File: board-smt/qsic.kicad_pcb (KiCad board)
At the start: 4 copper layers, 214.1 x 131.7 mm, 243 parts, among them CON1 SD 0, CON2 SD 1, P1 USB_A, P2 Indicator Panel, Q201 Dual_NMOS, Q202 Dual_NMOS, Q203 Dual_NMOS, Q204 Dual_NMOS, Q205 Dual_NMOS, Q206 Dual_NMOS, Q207 Dual_NMOS, Q208 Dual_NMOS, Q209 Dual_NMOS, Q210 Dual_NMOS, Q211 Dual_NMOS, Q212 Dual_NMOS, Q301 Dual_NMOS, Q302 Dual_NMOS, Q303 Dual_NMOS, Q304 Dual_NMOS, Q305 Dual_NMOS, Q306 Dual_NMOS, Q307 Dual_NMOS, U201 CMP401, U202 CMP401, U203 CMP401, U204 CMP401, U205 CMP401, U206 CMP401, U301 CMP401, U302 CMP401, U303 CMP401, U304 CMP401, U305 CMP401, U306 AOZ3010PI, U307 AOZ3010PI, U308 RT8288A, U309 SC189, U401 XC7A75T-CSG324, U501 IS43TR16128B, U601 MAX3033E

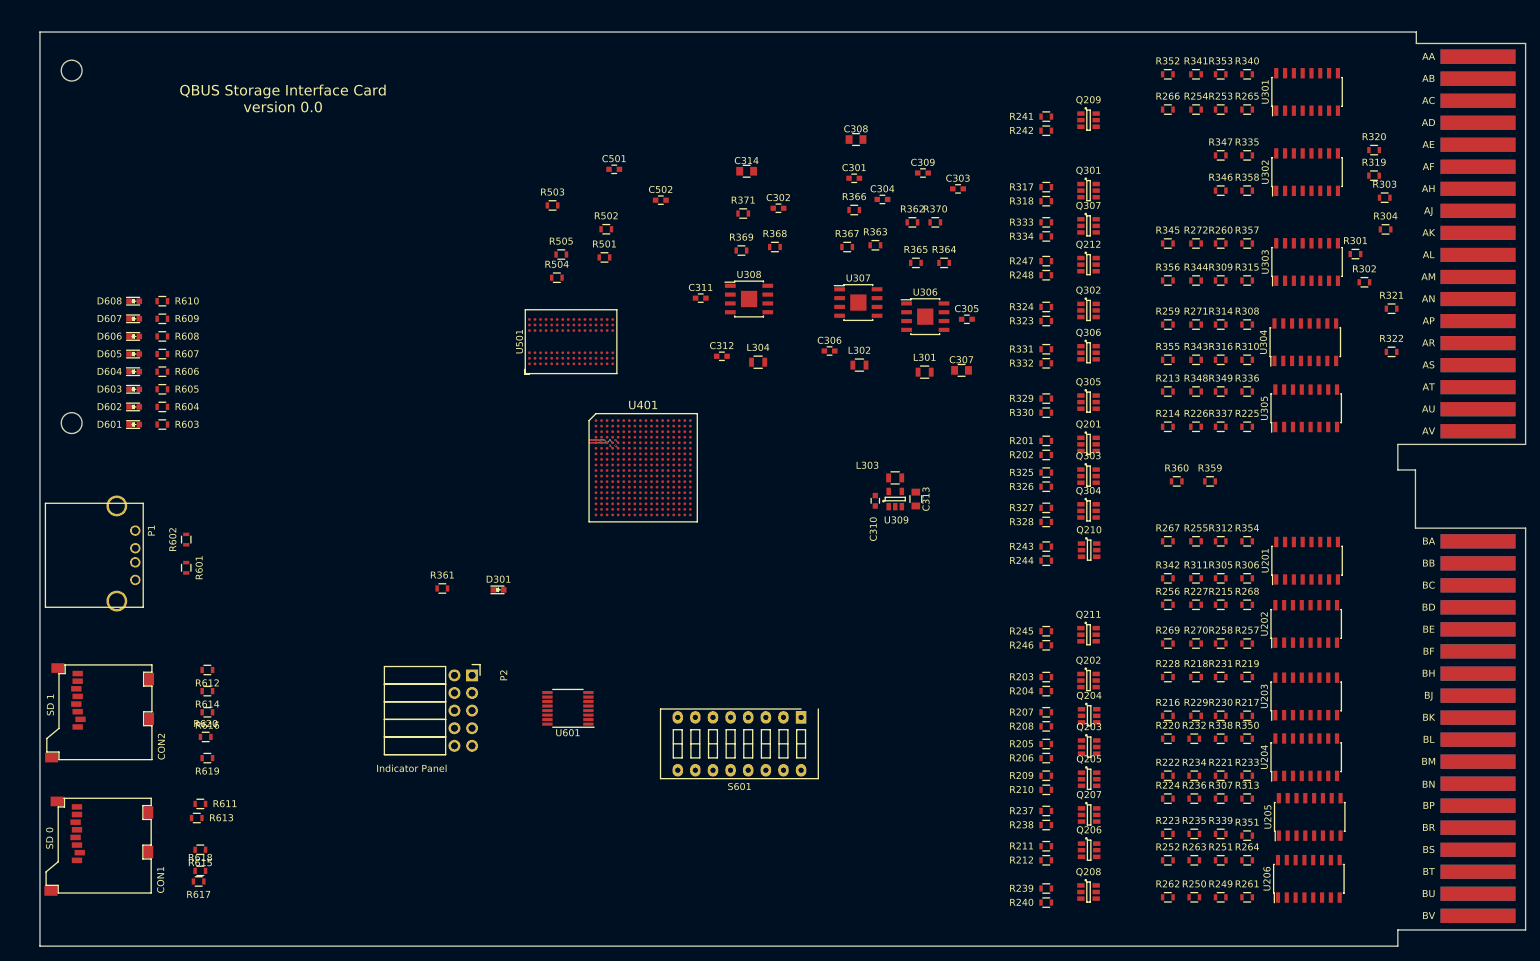
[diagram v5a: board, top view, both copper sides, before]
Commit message: Worked on the board layout for the bus receivers.
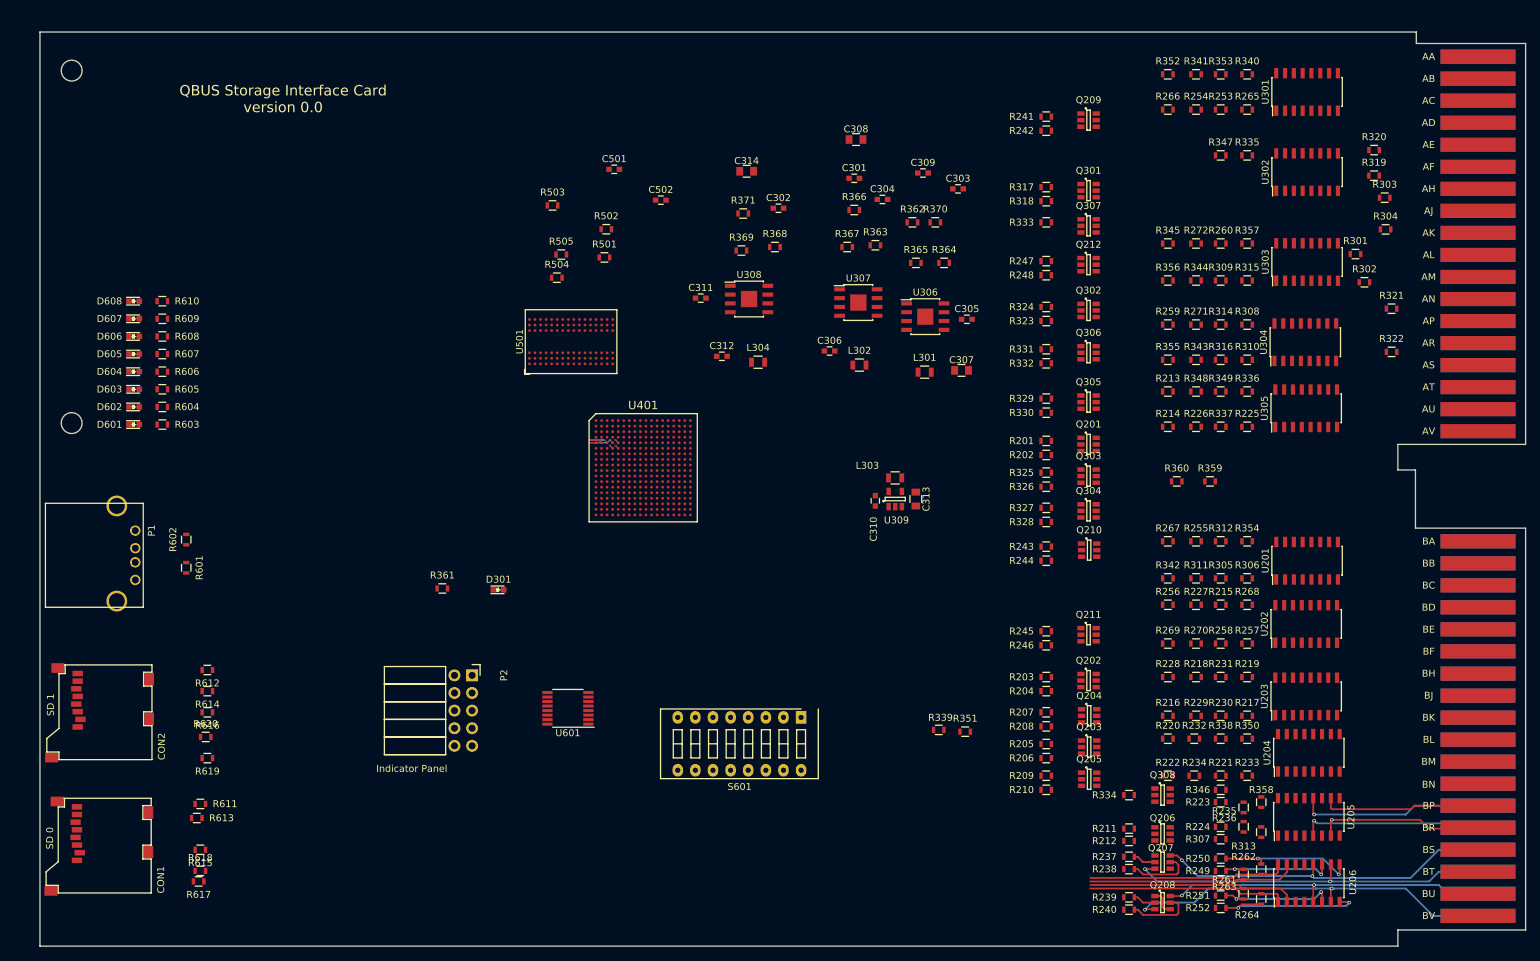
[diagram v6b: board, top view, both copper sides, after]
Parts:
- added Q308: Dual_NMOS, TO_SOT_Packages_SMD:SOT-23-6, F.Cu at (194.1, 135.4)
- moved R358 88.2 mm to (208.3, 136.4), turned to 270 degrees
- moved R346 86.4 mm to (202.4, 134.6), turned to 180 degrees
- moved R334 81.4 mm to (189.2, 135.4)
- moved R339 43.3 mm to (161.8, 126.0)
- moved R351 43.3 mm to (165.6, 126.2)
- moved R262 14.1 mm to (208.3, 146.1), turned to 270 degrees
- moved R237 13.6 mm to (189.2, 144.3)
- moved R238 13.5 mm to (189.2, 146.1)
- moved Q207 12.6 mm to (194.1, 145.0)
- moved R212 12.3 mm to (189.2, 142.0)
- moved R211 12.2 mm to (189.2, 140.2)
- moved R239 12.0 mm to (189.2, 150.1)
- moved R240 12.0 mm to (189.2, 151.9)
- moved Q206 10.8 mm to (194.1, 141.0)
- moved Q208 10.8 mm to (194.1, 150.9)
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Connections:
- Q307 pad 3: /Bus Control/BIRQ7 -> (no net)
- Q307 pad 4: GND -> (no net)
- Q307 pad 5: Net-(Q307-Pad5) -> (no net)
- R334 pad 1: Net-(Q307-Pad5) -> Net-(Q308-Pad2)
- U205 pad 1: /RREF -> /REVNT
- U205 pad 10: /Bus Control/BEVNT -> /Bus Control/BIRQ7
- U205 pad 11: Net-(R224-Pad1) -> Net-(R223-Pad1)
- U205 pad 12: /BDAL11 -> /BDAL10
- U205 pad 15: /Address/Data/RDAL11 -> /Address/Data/RDAL10
- U205 pad 16: /REVNT -> /RIRQ7
- U205 pad 2: /Address/Data/RDAL10 -> /Address/Data/RDAL11
- U205 pad 5: /BDAL10 -> /BDAL11
- U205 pad 6: Net-(R223-Pad1) -> Net-(R224-Pad1)
- U205 pad 7: /Bus Control/BREF -> /Bus Control/BEVNT
- U205 pad 8: Net-(R339-Pad1) -> Net-(R307-Pad2)
- U205 pad 9: Net-(R307-Pad2) -> Net-(R346-Pad1)
- U206 pad 1: /Address/Data/RDAL13 -> /Address/Data/RDAL15
- U206 pad 10: /BDAL14 -> /BDAL13
- U206 pad 11: Net-(R252-Pad1) -> Net-(R249-Pad1)
- U206 pad 12: /BDAL15 -> /BDAL12
- U206 pad 15: /Address/Data/RDAL15 -> /Address/Data/RDAL12
- U206 pad 16: /Address/Data/RDAL14 -> /Address/Data/RDAL13
- U206 pad 2: /Address/Data/RDAL12 -> /Address/Data/RDAL14
- U206 pad 5: /BDAL12 -> /BDAL14
- U206 pad 6: Net-(R249-Pad1) -> Net-(R251-Pad1)
- U206 pad 7: /BDAL13 -> /BDAL15
- U206 pad 8: Net-(R250-Pad1) -> Net-(R252-Pad1)
- U206 pad 9: Net-(R251-Pad1) -> Net-(R250-Pad1)
- U302 pad 2: /RIRQ7 -> /RREF
- U302 pad 5: /Bus Control/BIRQ7 -> /Bus Control/BREF
- U302 pad 6: Net-(R346-Pad1) -> Net-(R339-Pad1)
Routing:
- net /BDAL15: track 0.00 -> 54.5 mm, vias 0 -> 2
- net /BDAL13: track 0.00 -> 53.5 mm, vias 0 -> 2
- net /BDAL12: track 0.00 -> 49.3 mm, vias 0 -> 2
- net /BDAL14: track 0.00 -> 48.2 mm, vias 0 -> 2
- net /Address/Data/RDAL14: track 0.00 -> 29.9 mm
- net /Address/Data/RDAL12: track 0.00 -> 29.9 mm
- net /Address/Data/RDAL15: track 0.00 -> 28.9 mm
- net /Address/Data/RDAL13: track 0.00 -> 28.4 mm
- net /BDAL10: track 0.00 -> 26.6 mm, vias 0 -> 1
- net /BDAL11: track 0.00 -> 26.3 mm, vias 0 -> 1
- net /Bus Control/BEVNT: track 0.00 -> 23.8 mm, vias 0 -> 1
- net Net-(R252-Pad1): track 0.00 -> 23.1 mm, vias 0 -> 2
- net /Bus Control/BIRQ7: track 0.00 -> 22.9 mm
- net Net-(R250-Pad1): track 0.00 -> 19.8 mm, vias 0 -> 2
- net Net-(R249-Pad1): track 0.00 -> 16.9 mm, vias 0 -> 2
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
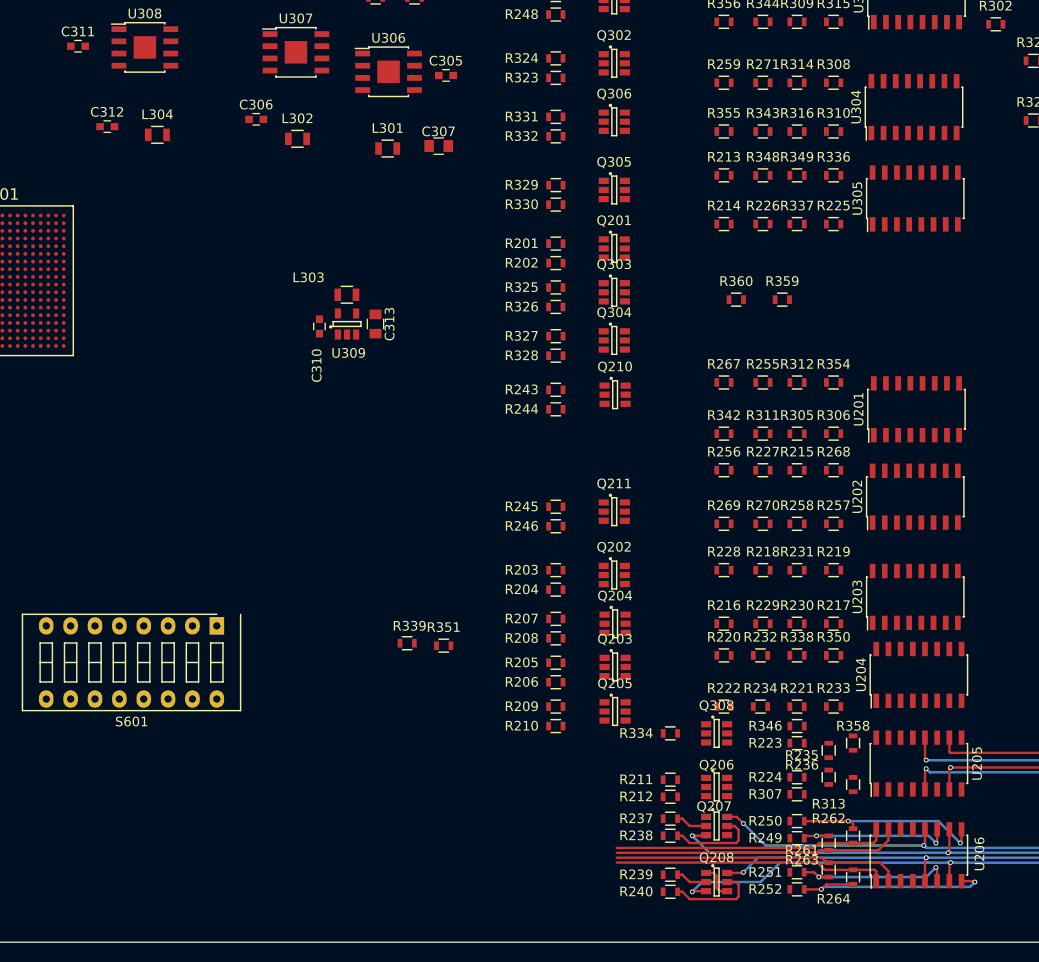
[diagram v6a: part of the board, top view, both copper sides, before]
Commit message: Moved comparator power connections to separate symbols.
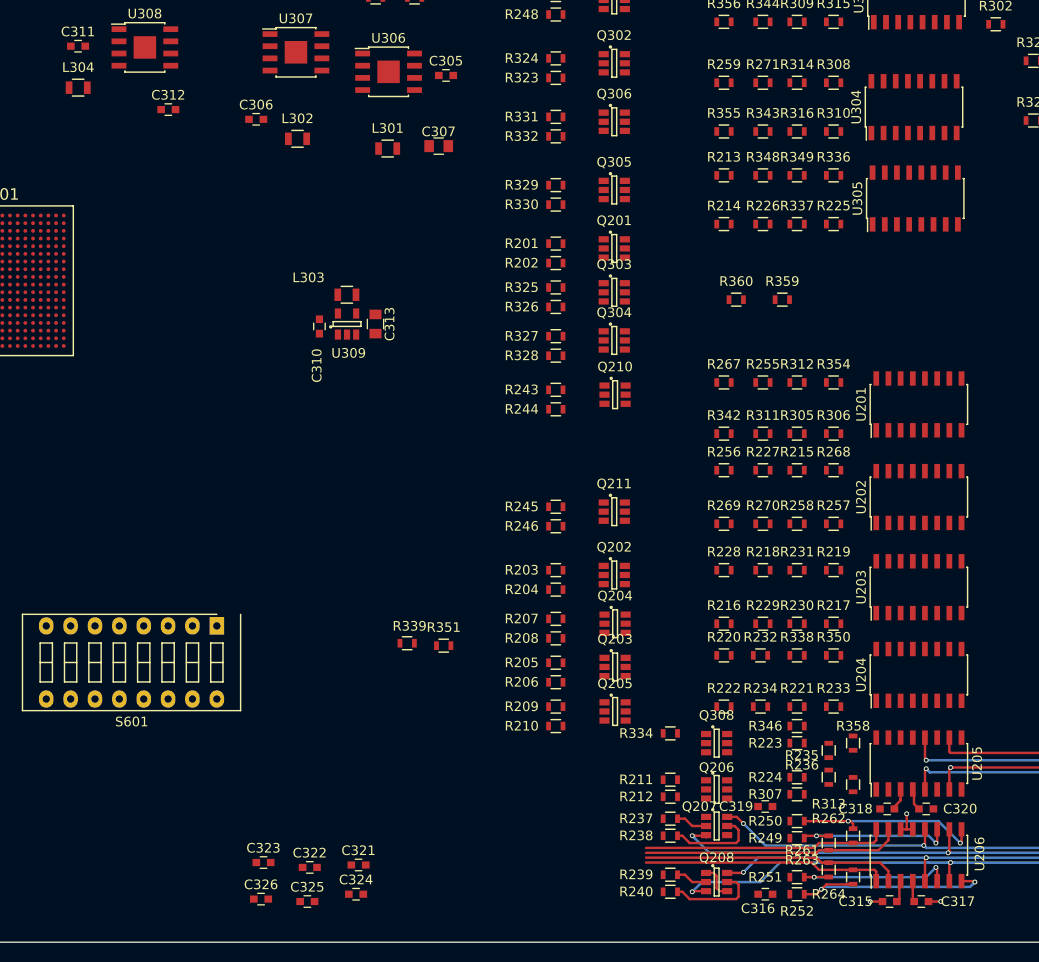
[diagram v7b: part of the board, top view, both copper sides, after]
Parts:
- added C315: 100nF, Capacitors_SMD:C_0603, F.Cu at (212.1, 152.9)
- added C316: 100nF, Capacitors_SMD:C_0603, F.Cu at (199.1, 152.1)
- added C317: 100nF, Capacitors_SMD:C_0603, F.Cu at (215.4, 152.9)
- added C318: 100nF, Capacitors_SMD:C_0603, F.Cu at (211.8, 143.3)
- added C319: 100nF, Capacitors_SMD:C_0603, F.Cu at (199.1, 143.0)
- added C320: 100nF, Capacitors_SMD:C_0603, F.Cu at (215.9, 143.3)
- added C321: 100nF, Capacitors_SMD:C_0603, F.Cu at (156.7, 149.1)
- added C322: 100nF, Capacitors_SMD:C_0603, F.Cu at (151.7, 149.4)
- added C323: 100nF, Capacitors_SMD:C_0603, F.Cu at (146.8, 148.8)
- added C324: 100nF, Capacitors_SMD:C_0603, F.Cu at (156.5, 152.1)
- added C325: 100nF, Capacitors_SMD:C_0603, F.Cu at (151.4, 152.9)
- added C326: 100nF, Capacitors_SMD:C_0603, F.Cu at (146.6, 152.7)
- R335, R336: value R -> 20kΩ
- R347, R348: value R -> 340kΩ
- moved L304 9.61 mm to (127.5, 68.1)
- moved C312 6.61 mm to (136.9, 70.4)
- moved U203 1.09 mm to (215.1, 120.1)
- moved Q308 1.02 mm to (194.1, 136.4)
- moved U201 0.57 mm to (215.1, 101.1)
- moved R251 0.51 mm to (202.4, 150.4)
- moved R252 0.51 mm to (202.4, 152.1)
- moved U202 0.38 mm to (215.1, 110.7)
- moved Q206 0.25 mm to (194.1, 141.2)
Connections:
- R202 pad 1: Net-(Q201-Pad5) -> /Address/Data/TDAL1
- R202 pad 2: /Address/Data/TDAL1 -> Net-(Q201-Pad5)
- R219 pad 1: Net-(R219-Pad1) -> +1V5
- R219 pad 2: +1V5 -> Net-(R219-Pad2)
- R231 pad 1: Net-(R219-Pad1) -> Net-(R219-Pad2)
- R235 pad 2: /Address/Data/RDAL10 -> Net-(R235-Pad2)
- R262 pad 1: Net-(R250-Pad1) -> /Address/Data/RDAL13
- R262 pad 2: /Address/Data/RDAL13 -> Net-(R250-Pad1)
- R311 pad 1: Net-(R305-Pad2) -> /RPOK
- R311 pad 2: /RPOK -> Net-(R305-Pad2)
- R312 pad 1: Net-(R306-Pad2) -> /RDCOK
- R312 pad 2: /RDCOK -> Net-(R306-Pad2)
- R313 pad 1: Net-(R307-Pad2) -> /REVNT
- R313 pad 2: /REVNT -> Net-(R307-Pad2)
- R314 pad 1: Net-(R308-Pad2) -> /RHALT
- R314 pad 2: /RHALT -> Net-(R308-Pad2)
- R315 pad 1: Net-(R309-Pad2) -> /RIAKI
- R315 pad 2: /RIAKI -> Net-(R309-Pad2)
- R316 pad 1: Net-(R310-Pad2) -> /RDMGI
- R316 pad 2: /RDMGI -> Net-(R310-Pad2)
- R355 pad 1: Net-(R343-Pad1) -> /RIRQ4
- R355 pad 2: /RIRQ4 -> Net-(R343-Pad1)
- R356 pad 1: Net-(R344-Pad1) -> /RIRQ5
- R356 pad 2: /RIRQ5 -> Net-(R344-Pad1)
- R357 pad 1: Net-(R345-Pad1) -> /RIRQ6
- R357 pad 2: /RIRQ6 -> Net-(R345-Pad1)
- R358 pad 1: Net-(R346-Pad1) -> /RIRQ7
- R358 pad 2: /RIRQ7 -> Net-(R346-Pad1)
- R601 pad 1: /I/O/USB_D+ -> /I/O/USB_D-
- R602 pad 1: /I/O/USB_D- -> /I/O/USB_D+
- U203 pad 9: Net-(R219-Pad1) -> Net-(R219-Pad2)
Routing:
- net /Address/Data/RDAL13: track 28.4 -> 1.51 mm
- net Net-(R250-Pad1): track 19.8 -> 43.7 mm
- net GND: track 7.26 -> 12.7 mm, vias 1 -> 4
- net +3V3: track 0.00 -> 4.60 mm
- net +5V: track 0.00 -> 4.48 mm
- net /Address/Data/RDAL14: track 29.9 -> 26.9 mm
- net /Address/Data/RDAL15: track 28.9 -> 25.8 mm
- net /Address/Data/RDAL12: track 29.9 -> 26.8 mm

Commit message: Little fixups
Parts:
- P2: footprint Socket_Strips:Socket_Strip_Angled_2x05 -> Pin_Headers:Pin_Header_Angled_2x05
- moved D601 24.3 mm to (53.8, 59.0)
- moved R603 24.3 mm to (57.9, 59.0)
- moved D602 24.3 mm to (53.8, 56.4)
- moved D604 24.3 mm to (53.8, 51.4)
- moved D606 24.3 mm to (53.8, 46.3)
- moved D608 24.3 mm to (53.8, 41.2)
- moved R604 24.3 mm to (57.9, 56.4)
- moved R606 24.3 mm to (57.9, 51.4)
- moved R608 24.3 mm to (57.9, 46.3)
- moved R610 24.3 mm to (57.9, 41.2)
- moved D603 24.3 mm to (53.8, 53.9)
- moved D605 24.3 mm to (53.8, 48.8)
- moved D607 24.3 mm to (53.8, 43.7)
- moved R605 24.3 mm to (57.9, 53.9)
- moved R607 24.3 mm to (57.9, 48.8)
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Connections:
- net VDD renamed Net-(U601-Pad16)
- R213 pad 2: +1V5 -> +1V5_ref
- R214 pad 2: +1V5 -> +1V5_ref
- R215 pad 2: +1V5 -> +1V5_ref
- R216 pad 2: +1V5 -> +1V5_ref
- R217 pad 2: +1V5 -> +1V5_ref
- R218 pad 2: +1V5 -> +1V5_ref
- R219 pad 1: +1V5 -> +1V5_ref
- R220 pad 2: +1V5 -> +1V5_ref
- R221 pad 2: +1V5 -> +1V5_ref
- R222 pad 2: +1V5 -> +1V5_ref
- R223 pad 2: +1V5 -> +1V5_ref
- R224 pad 2: +1V5 -> +1V5_ref
- R249 pad 2: +1V5 -> +1V5_ref
- R250 pad 2: +1V5 -> +1V5_ref
- R251 pad 2: +1V5 -> +1V5_ref
- R252 pad 2: +1V5 -> +1V5_ref
- R253 pad 2: +1V5 -> +1V5_ref
- R254 pad 2: +1V5 -> +1V5_ref
- R255 pad 2: +1V5 -> +1V5_ref
- R256 pad 2: +1V5 -> +1V5_ref
- R257 pad 2: +1V5 -> +1V5_ref
- R258 pad 2: +1V5 -> +1V5_ref
- R259 pad 2: +1V5 -> +1V5_ref
- R260 pad 2: +1V5 -> +1V5_ref
- R305 pad 1: +1V5 -> +1V5_ref
- R306 pad 1: +1V5 -> +1V5_ref
- R307 pad 1: +1V5 -> +1V5_ref
- R308 pad 1: +1V5 -> +1V5_ref
- R335 pad 2: +1V5 -> +1V5_ref
- R336 pad 2: +1V5 -> +1V5_ref
- R337 pad 2: +1V5 -> +1V5_ref
- R338 pad 2: +1V5 -> +1V5_ref
- R339 pad 2: +1V5 -> +1V5_ref
- R340 pad 2: +1V5 -> +1V5_ref
- R341 pad 2: +1V5 -> +1V5_ref
- R342 pad 2: +1V5 -> +1V5_ref
- R343 pad 2: +1V5 -> +1V5_ref
- R344 pad 2: +1V5 -> +1V5_ref
- R345 pad 2: +1V5 -> +1V5_ref
- R346 pad 2: +1V5 -> +1V5_ref
- R359 pad 1: +1V5 -> +1V5_ref
- U601 pad 8: GND -> Net-(U601-Pad8)
